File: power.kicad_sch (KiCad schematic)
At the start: 26 parts, among them U3 EA3036

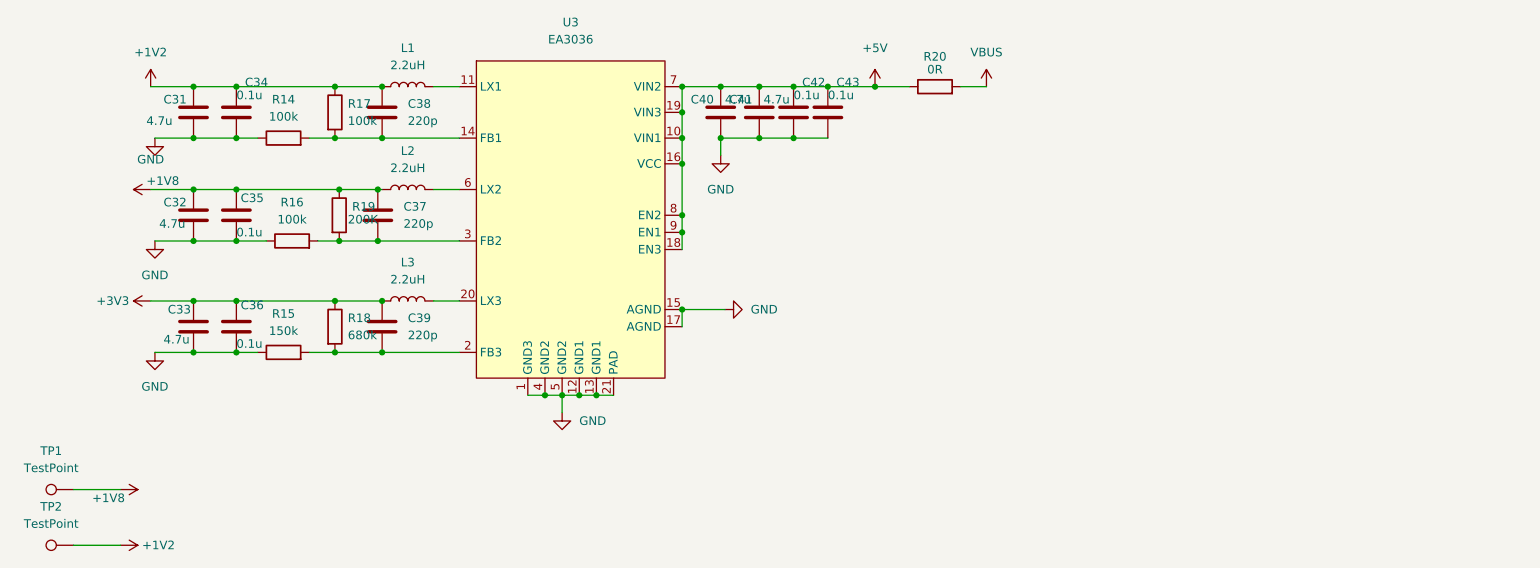
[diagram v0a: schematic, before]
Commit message: use LDO to produce 1.2V, to fix fpga voltage issue. fix wrong fpga sch issue, change the pins of fpga. connect fpga SSPI to V3s-spi, so that we can configuare fpag on v3s someday.
Signed-off-by: ncerzzk <huangzzk@bupt.edu.cn>
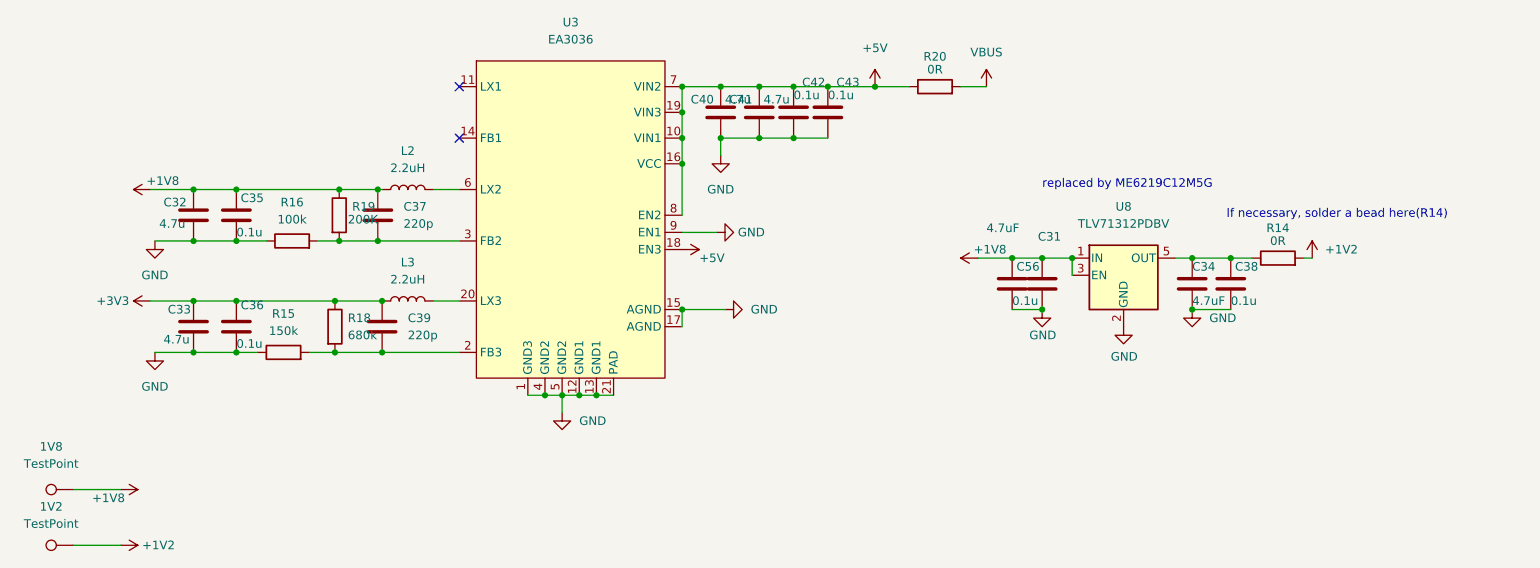
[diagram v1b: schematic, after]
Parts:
- removed L1: 2.2uH, Inductor_SMD:L_Abracon_ASPI-3012S, symbol Device:L
- removed R17: 100k, Resistor_SMD:R_0402_1005Metric, symbol Device:R
- added C56: 0.1u, Capacitor_SMD:C_0402_1005Metric, symbol Device:C
- added U8: TLV71312PDBV, Package_TO_SOT_SMD:SOT-23-5, symbol Regulator_Linear:TLV71312PDBV
- C31: value 4.7u -> 4.7uF
- C34: value 0.1u -> 4.7uF
- C38: value 220p -> 0.1u
- R14: value 100k -> 0R
- renumbered TP2 to 1V2, TP1 to 1V8
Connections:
- net +1V2: now also R14.2; no longer C31.1, C34.1, C38.1
- net +1V8: now also C31.1, C56.1, U8.1 (IN), U8.3 (EN)
- net +5V: no longer U3.9 (EN1)
- net GND: now also C38.2, U3.9 (EN1), C56.2, U8.2 (GND); no longer R14.1
- new net: C34.1, C38.1, R14.1, U8.5 (OUT)
- now unconnected: U3.14 (FB1)
- no-connect marks 0 -> 2
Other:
- note added: "If necessary, solder a bead here(R14)"
- note added: "replaced by ME6219C12M5G"

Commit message: v1.0
Signed-off-by: ncerzzk <huangzzk@bupt.edu.cn>
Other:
- note added: "replaced by ME6212C12M5G"
- note removed: "replaced by ME6219C12M5G"
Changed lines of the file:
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@@
     (stroke (width 0) (type default) (color 0 0 0 0))
   )
-  (text "replaced by ME6219C12M5G" (at 274.32 138.43 0)
+  (text "replaced by ME6212C12M5G" (at 274.32 138.43 0)
     (effects (font (size 1.27 1.27)) (justify left bottom))
   )

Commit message: update 2.0
Signed-off-by: huangzzk <huangcmzzk@gmail.com>
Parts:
- removed C56: 0.1u, Capacitor_SMD:C_0402_1005Metric, symbol Device:C
- removed U8: TLV71312PDBV, Package_TO_SOT_SMD:SOT-23-5, symbol Regulator_Linear:TLV71312PDBV
- added L1: 2.2uH, Inductor_SMD:L_Abracon_ASPI-3012S, symbol Device:L
- added R17: 100K, Resistor_SMD:R_0402_1005Metric, symbol Device:R
- C31: value 4.7uF -> 4.7u
- C34: value 4.7uF -> 0.1u
- C38: value 0.1u -> 220p
- R14: value 0R -> 100k
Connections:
- net +1V2: now also C31.1, C34.1, C38.1, L1.1, R17.1; no longer R14.2
- net +1V8: no longer C31.1
- net +5V: now also U3.9 (EN1)
- net GND: now also R14.1; no longer C38.2, U3.9 (EN1)
- net at U3.11 (LX1): now also L1.2
- net at U3.14 (FB1): now also C38.2, R14.2, R17.2
- no-connect marks 2 -> 0
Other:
- note removed: "If necessary, solder a bead here(R14)"
- note removed: "replaced by ME6212C12M5G"
